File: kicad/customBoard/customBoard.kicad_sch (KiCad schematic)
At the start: 0 parts

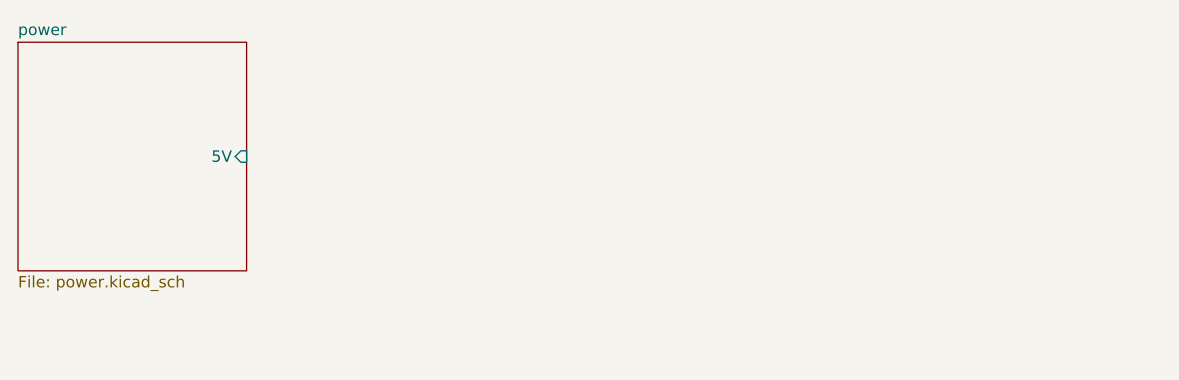
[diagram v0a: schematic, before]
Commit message: First draft of CM4_GPIO
The CM4 connectors are split into two units. This is the right unit, name GPIO. Next is the left, High Speed Serial unit.
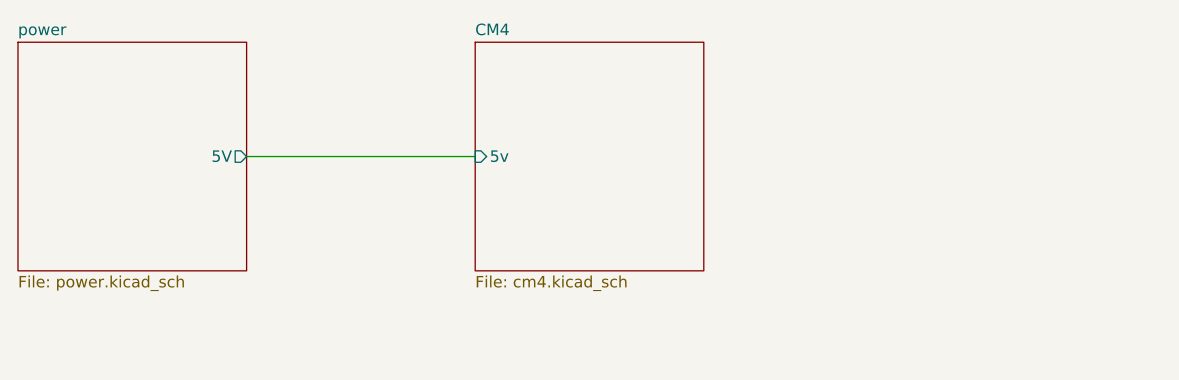
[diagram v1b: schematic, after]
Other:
- added sheet CM4 (cm4.kicad_sch)

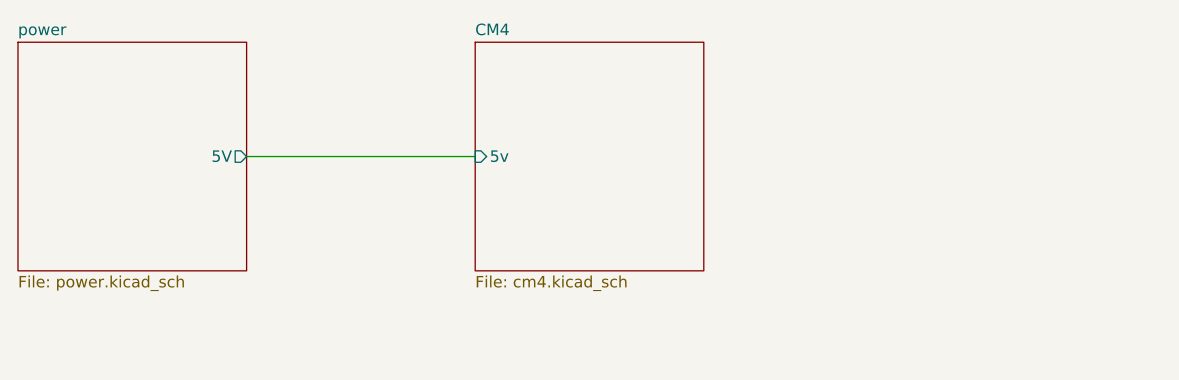
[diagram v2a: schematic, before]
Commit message: First draft of USB
This should complete the first draft of the schematic!
Now time to design the PCB itself
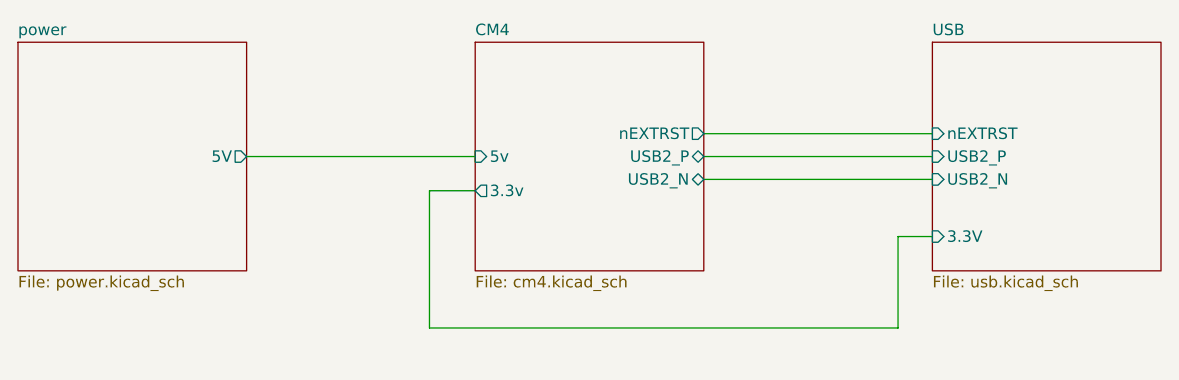
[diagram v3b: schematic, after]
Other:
- added sheet USB (usb.kicad_sch)
- sheet CM4 ports: added 3.3v, USB2_N, USB2_P, nEXTRST; removed none

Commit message: Generate Netlist
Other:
- sheet USB ports: added 3.3v, 5V; removed 3.3V
